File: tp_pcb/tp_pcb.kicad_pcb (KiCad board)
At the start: 2 copper layers, 66.5 x 76 mm, 26 parts, among them K0 KEYSW, K1 KEYSW, K2 KEYSW, K3 KEYSW, K4 KEYSW, K5 KEYSW, K6 KEYSW, P0 CONN_01X08, P1 CONN_01X08, P2 CONN_01X06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

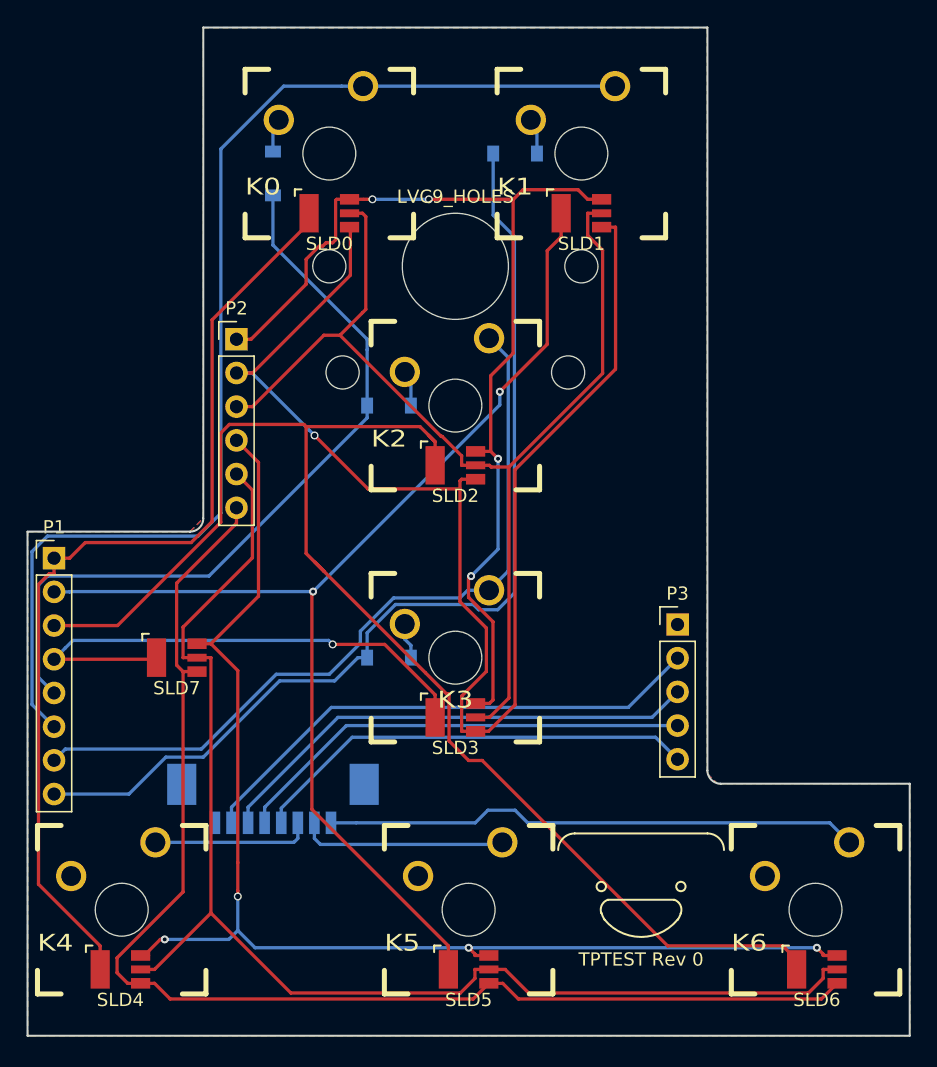
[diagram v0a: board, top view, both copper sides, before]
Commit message: working on mounting holes
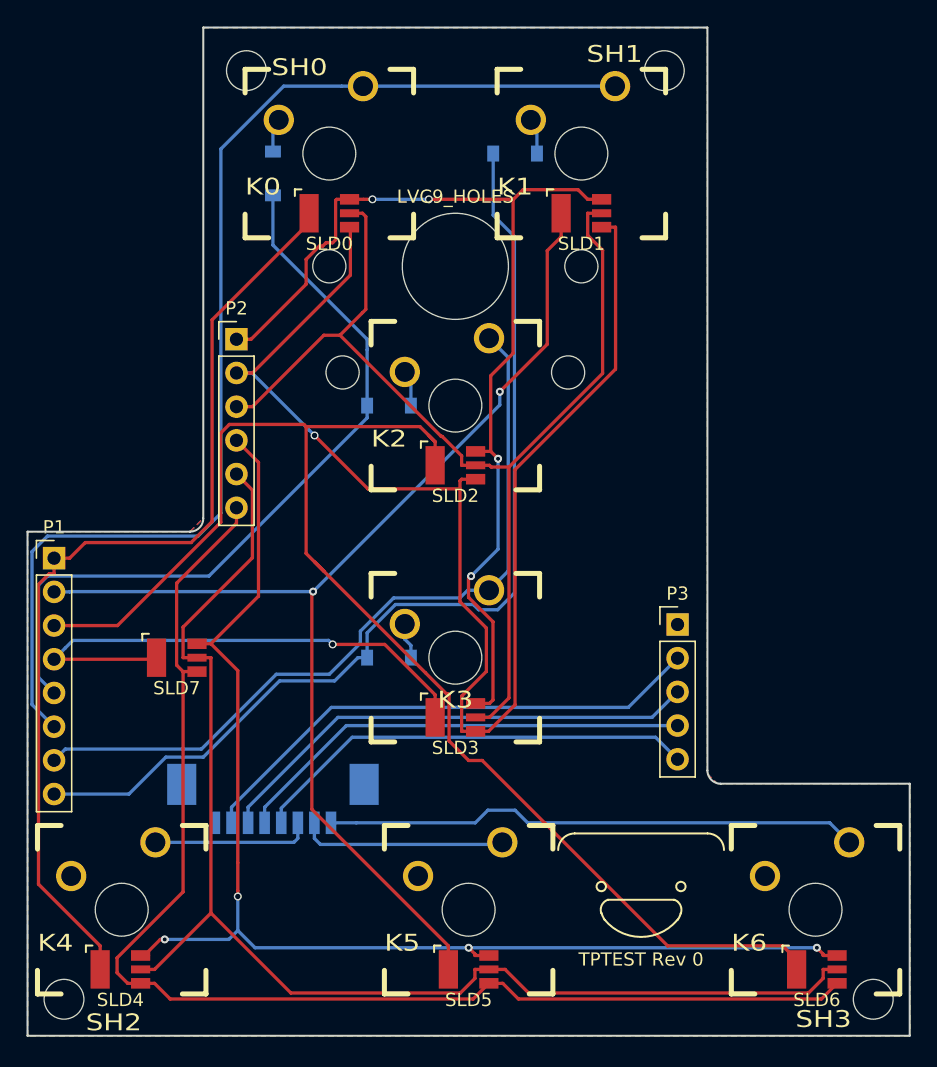
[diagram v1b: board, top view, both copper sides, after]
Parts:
- added SH0: CONN_01X01, cherry_rgb:MOUNTING_HOLE, F.Cu at (122.2, 36.8)
- added SH1: CONN_01X01, cherry_rgb:MOUNTING_HOLE, F.Cu at (153.8, 36.8)
- added SH2: CONN_01X01, cherry_rgb:MOUNTING_HOLE, F.Cu at (108.5, 106.8)
- added SH3: CONN_01X01, cherry_rgb:MOUNTING_HOLE, F.Cu at (169.5, 106.8)
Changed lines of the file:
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@@
     (tracks 308)
     (zones 0)
-    (modules 26)
+    (modules 30)
     (nets 27)
   )
@@
     (trace_clearance 0.2)
     (zone_clearance 0.25)
-    (zone_45_only no)
+    (zone_45_only yes)
     (trace_min 0.2)
     (segment_width 0.2)
@@
       (net 8 GND))
     (pad HOLE np_thru_hole circle (at 0 0) (size 3.9878 3.9878) (drill 3.9878) (layers *.Cu))
+  )
+  (module cherry_rgb:MOUNTING_HOLE (layer F.Cu)
+    (at 122.25 36.75)
+    (fp_text reference SH0 (at 4 -0.25) (layer F.SilkS)
+      (effects (font (size 1.27 1.524) (thickness 0.2032)))
+    )
+    (fp_text value CONN_01X01 (at 0 3.25) (layer F.SilkS) hide
+      (effects (font (size 1.27 1.524) (thickness 0.2032)))
+    )
+    (pad "" np_thru_hole circle (at 0 0) (size 3 3) (drill 3) (layers *.Cu))
+  )
+  (module cherry_rgb:MOUNTING_HOLE (layer F.Cu)
+    (at 153.75 36.75)
+    (fp_text reference SH1 (at -3.75 -1.25) (layer F.SilkS)
+      (effects (font (size 1.27 1.524) (thickness 0.2032)))
+    )
+    (fp_text value CONN_01X01 (at 0 3.25) (layer F.SilkS) hide
+      (effects (font (size 1.27 1.524) (thickness 0.2032)))
+    )
+    (pad "" np_thru_hole circle (at 0 0) (size 3 3) (drill 3) (layers *.Cu))
+  )
+  (module cherry_rgb:MOUNTING_HOLE (layer F.Cu)
+    (at 108.5 106.75)
+    (fp_text reference SH2 (at 3.75 1.75) (layer F.SilkS)
+      (effects (font (size 1.27 1.524) (thickness 0.2032)))
+    )
+    (fp_text value CONN_01X01 (at 0 3.25) (layer F.SilkS) hide
+      (effects (font (size 1.27 1.524) (thickness 0.2032)))
+    )
+    (pad "" np_thru_hole circle (at 0 0) (size 3 3) (drill 3) (layers *.Cu))
+  )
+  (module cherry_rgb:MOUNTING_HOLE (layer F.Cu)
+    (at 169.5 106.75)
+    (fp_text reference SH3 (at -3.75 1.5) (layer F.SilkS)
+      (effects (font (size 1.27 1.524) (thickness 0.2032)))
+    )
+    (fp_text value CONN_01X01 (at 0 3.25) (layer F.SilkS) hide
+      (effects (font (size 1.27 1.524) (thickness 0.2032)))
+    )
+    (pad "" np_thru_hole circle (at 0 0) (size 3 3) (drill 3) (layers *.Cu))
   )
   (gr_line (start 157 89.5) (end 157 33.5) (angle 90) (layer Edge.Cuts) (width 0.15))
@@
       )
     )
+  )
+  (zone (net 0) (net_name "") (layer F.Cu) (hatch edge 0.508)
+    (connect_pads (clearance 0.25))
+    (min_thickness 0.254)
+    (keepout (tracks allowed) (vias allowed) (copperpour not_allowed))
+    (fill yes (arc_segments 16) (thermal_gap 0.508) (thermal_bridge_width 0.508))
+    (polygon
+      (pts
+        (xy 121.25 35.5) (xy 121 35.75) (xy 119.25 34) (xy 119.5 33.75)
+      )
+    )
+  )
+  (zone (net 0) (net_name "") (layer B.Cu) (hatch edge 0.508)
+    (connect_pads (clearance 0.25))
+    (min_thickness 0.254)
+    (keepout (tracks allowed) (vias allowed) (copperpour not_allowed))
+    (fill yes (arc_segments 16) (thermal_gap 0.508) (thermal_bridge_width 0.508))
+    (polygon
+      (pts
+        (xy 121.25 35.5) (xy 121 35.75) (xy 119.25 34) (xy 119.5 33.75)
+      )
+    )
+  )
+  (zone (net 0) (net_name "") (layer B.Cu) (hatch edge 0.508)
+    (connect_pads (clearance 0.25))
+    (min_thickness 0.254)
+    (keepout (tracks allowed) (vias allowed) (copperpour not_allowed))
+    (fill yes (arc_segments 16) (thermal_gap 0.508) (thermal_bridge_width 0.508))
+    (polygon
+      (pts
+        (xy 156.75 34) (xy 155 35.75) (xy 154.75 35.5) (xy 156.5 33.75)
+      )
+    )
+  )
+  (zone (net 0) (net_name "") (layer F.Cu) (hatch edge 0.508)
+    (connect_pads (clearance 0.25))
+    (min_thickness 0.254)
+    (keepout (tracks allowed) (vias allowed) (copperpour not_allowed))
+    (fill yes (arc_segments 16) (thermal_gap 0.508) (thermal_bridge_width 0.508))
+    (polygon
+      (pts
+        (xy 156.75 34) (xy 155 35.75) (xy 154.75 35.5) (xy 156.5 33.75)
+      )
+    )
+  )
+  (zone (net 0) (net_name "") (layer B.Cu) (hatch edge 0.508)
+    (connect_pads (clearance 0.25))
+    (min_thickness 0.254)
+    (keepout (tracks allowed) (vias allowed) (copperpour not_allowed))
+    (fill yes (arc_segments 16) (thermal_gap 0.508) (thermal_bridge_width 0.508))
+    (polygon
+      (pts
+        (xy 106 109) (xy 106.25 109.25) (xy 108 107.5) (xy 107.75 107.25)
+      )
+    )
+  )
+  (zone (net 0) (net_name "") (layer B.Cu) (hatch edge 0.508)
+    (connect_pads (clearance 0.25))
+    (min_thickness 0.254)
+    (keepout (tracks allowed) (vias allowed) (copperpour not_allowed))
+    (fill yes (arc_segments 16) (thermal_gap 0.508) (thermal_bridge_width 0.508))
+    (polygon
+      (pts
+        (xy 171.75 109.25) (xy 172 109) (xy 170.25 107.25) (xy 170 107.5)
+      )
+    )

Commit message: tp adjusted mounting hole text
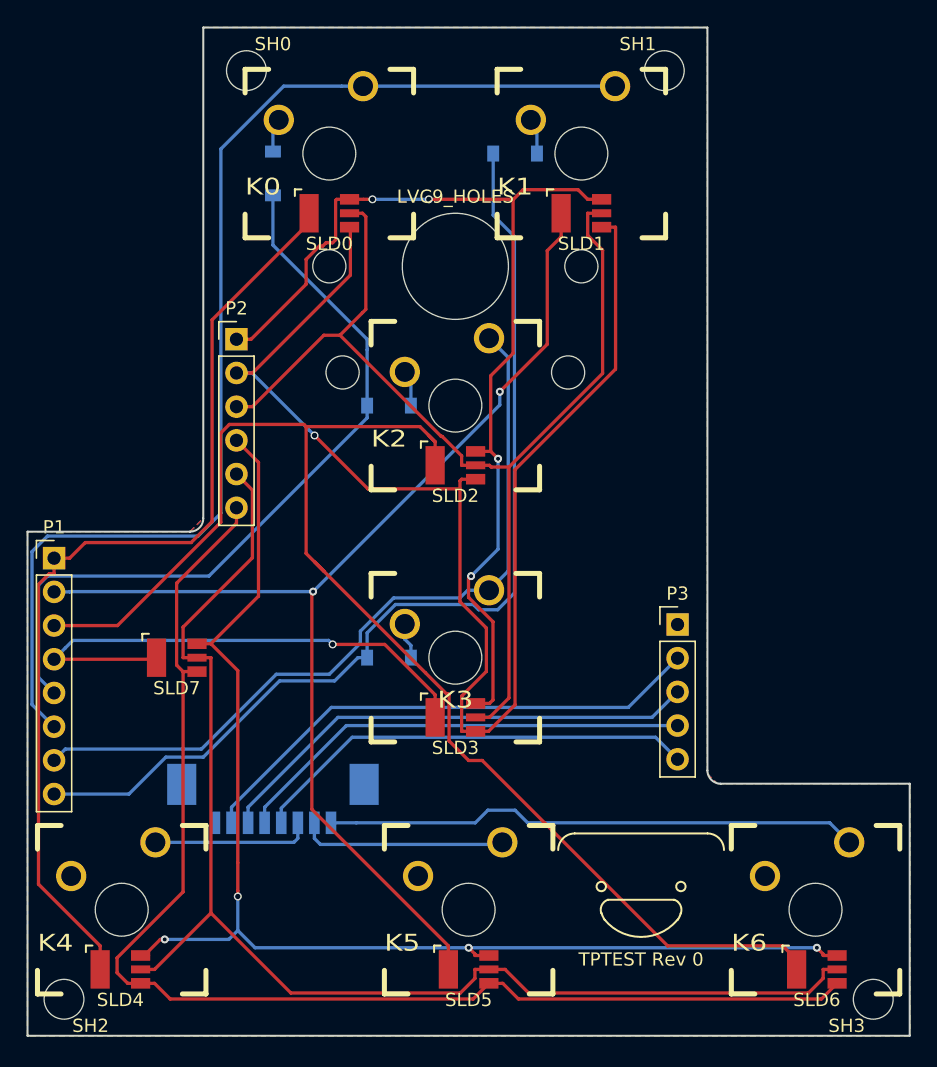
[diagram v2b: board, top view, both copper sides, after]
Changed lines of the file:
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@@
   (module cherry_rgb:MOUNTING_HOLE (layer F.Cu)
     (at 122.25 36.75)
-    (fp_text reference SH0 (at 4 -0.25) (layer F.SilkS)
-      (effects (font (size 1.27 1.524) (thickness 0.2032)))
+    (fp_text reference SH0 (at 2 -2) (layer F.SilkS)
+      (effects (font (size 1 1) (thickness 0.2)))
     )
     (fp_text value CONN_01X01 (at 0 3.25) (layer F.SilkS) hide
@@
   (module cherry_rgb:MOUNTING_HOLE (layer F.Cu)
     (at 153.75 36.75)
-    (fp_text reference SH1 (at -3.75 -1.25) (layer F.SilkS)
-      (effects (font (size 1.27 1.524) (thickness 0.2032)))
+    (fp_text reference SH1 (at -2 -2) (layer F.SilkS)
+      (effects (font (size 1 1) (thickness 0.2)))
     )
     (fp_text value CONN_01X01 (at 0 3.25) (layer F.SilkS) hide
@@
   (module cherry_rgb:MOUNTING_HOLE (layer F.Cu)
     (at 108.5 106.75)
-    (fp_text reference SH2 (at 3.75 1.75) (layer F.SilkS)
-      (effects (font (size 1.27 1.524) (thickness 0.2032)))
+    (fp_text reference SH2 (at 2 2) (layer F.SilkS)
+      (effects (font (size 1 1) (thickness 0.2)))
     )
     (fp_text value CONN_01X01 (at 0 3.25) (layer F.SilkS) hide
@@
   (module cherry_rgb:MOUNTING_HOLE (layer F.Cu)
     (at 169.5 106.75)
-    (fp_text reference SH3 (at -3.75 1.5) (layer F.SilkS)
-      (effects (font (size 1.27 1.524) (thickness 0.2032)))
+    (fp_text reference SH3 (at -2 2) (layer F.SilkS)
+      (effects (font (size 1 1) (thickness 0.2)))
     )
     (fp_text value CONN_01X01 (at 0 3.25) (layer F.SilkS) hide

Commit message: tp groundplanes seem done
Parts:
- added V0: CONN_01X01, cherry_rgb:VIA127, F.Cu at (144.0, 63.0)
- added V1: CONN_01X01, cherry_rgb:VIA127, F.Cu at (136.8, 78.2)
- added V2: CONN_01X01, cherry_rgb:VIA127, F.Cu at (118.2, 99.5)
- added V3: CONN_01X01, cherry_rgb:VIA127, F.Cu at (142.0, 78.5)
- moved P1 0.35 mm to (108.0, 73.2)
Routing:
- net red1: track 97.6 -> 113.9 mm
- net red0: track 82.5 -> 90.6 mm
- net c1: track 76.2 -> 78.1 mm
- net blue0: track 78.2 -> 80.1 mm
- net a0: track 73.0 -> 74.2 mm
- net a2: track 105.0 -> 106.0 mm
- net a3: track 40.5 -> 39.9 mm
